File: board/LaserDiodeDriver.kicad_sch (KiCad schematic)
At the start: 55 parts, among them J1 Conn_01x02, K1 EE2-12NU, Q1 2N7002, Q2 IRF9Z34, SW1 SW_SPDT, U1 LT1009, U2 OPA4192, U3 LM317

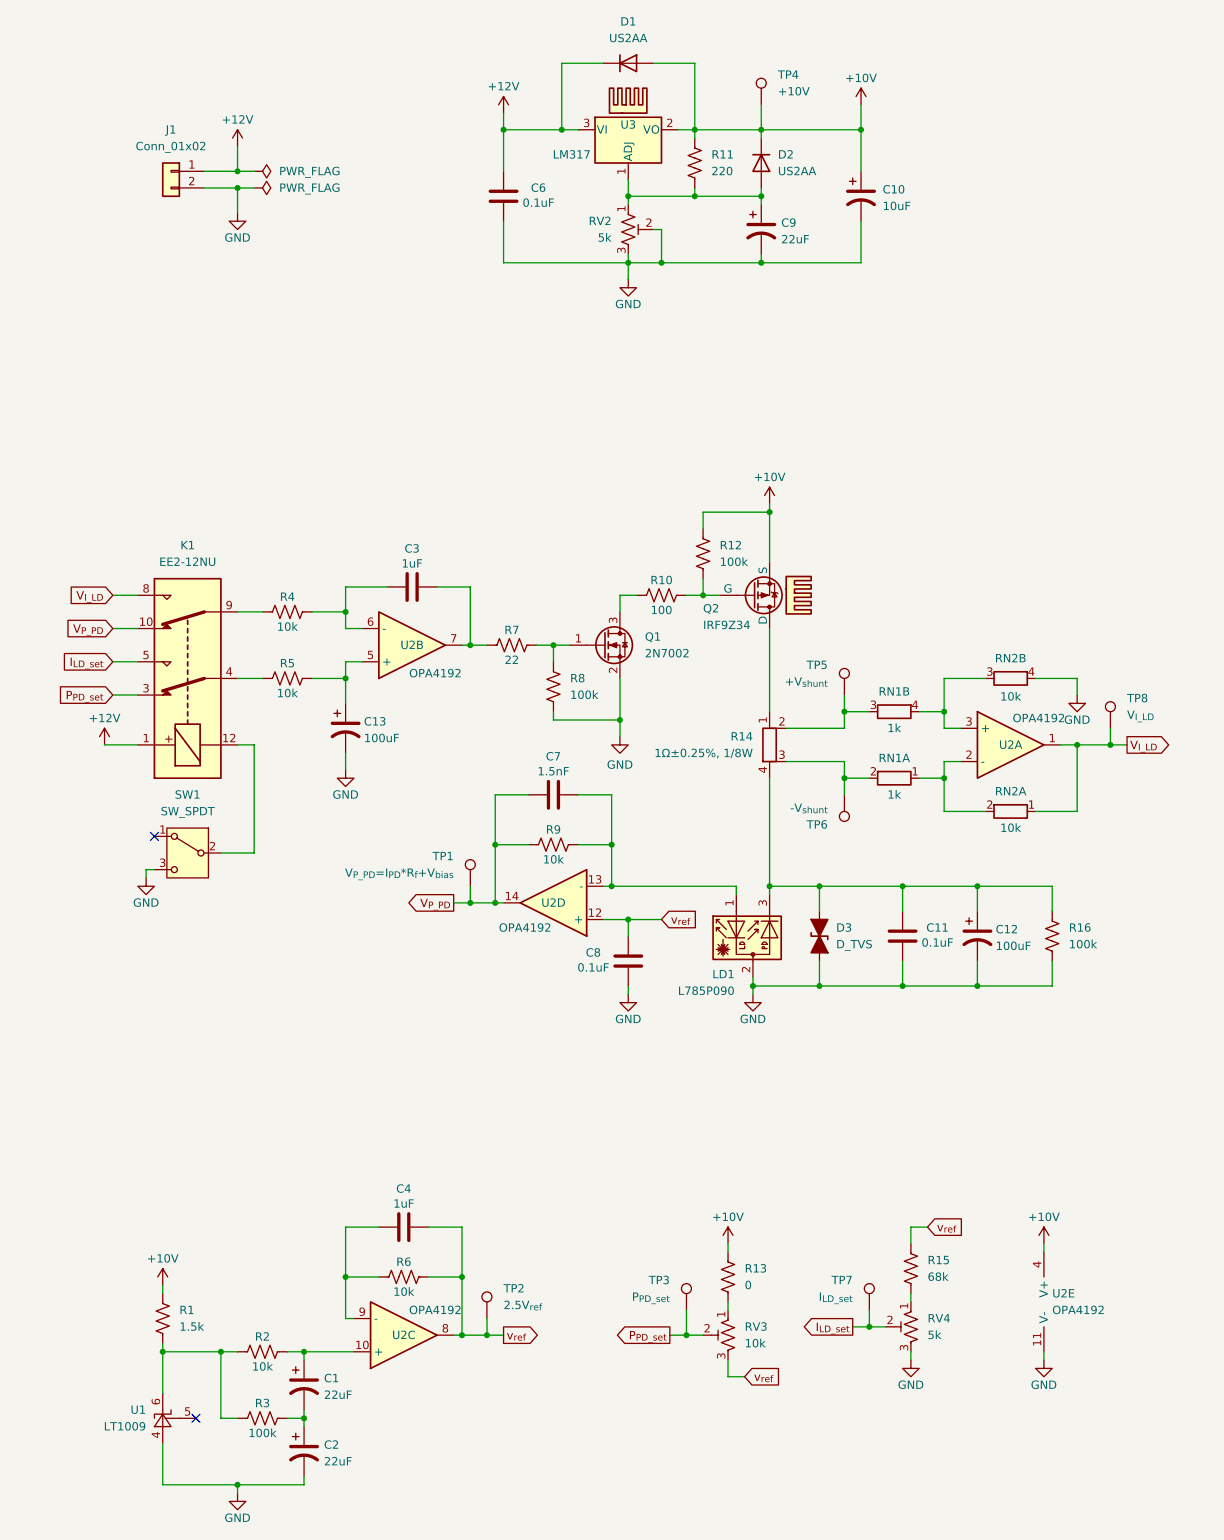
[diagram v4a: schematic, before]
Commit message: Various changes + component placement
* Removed signal relay in favor of SPDT switch in the interest of space.
* Placed components for optimal mechanical mounting with LD in center of PCB.
* Got rid of LM317 pot for space calculated proper values for LM317 to be +10V output.
* Arranged resistors for good placement.
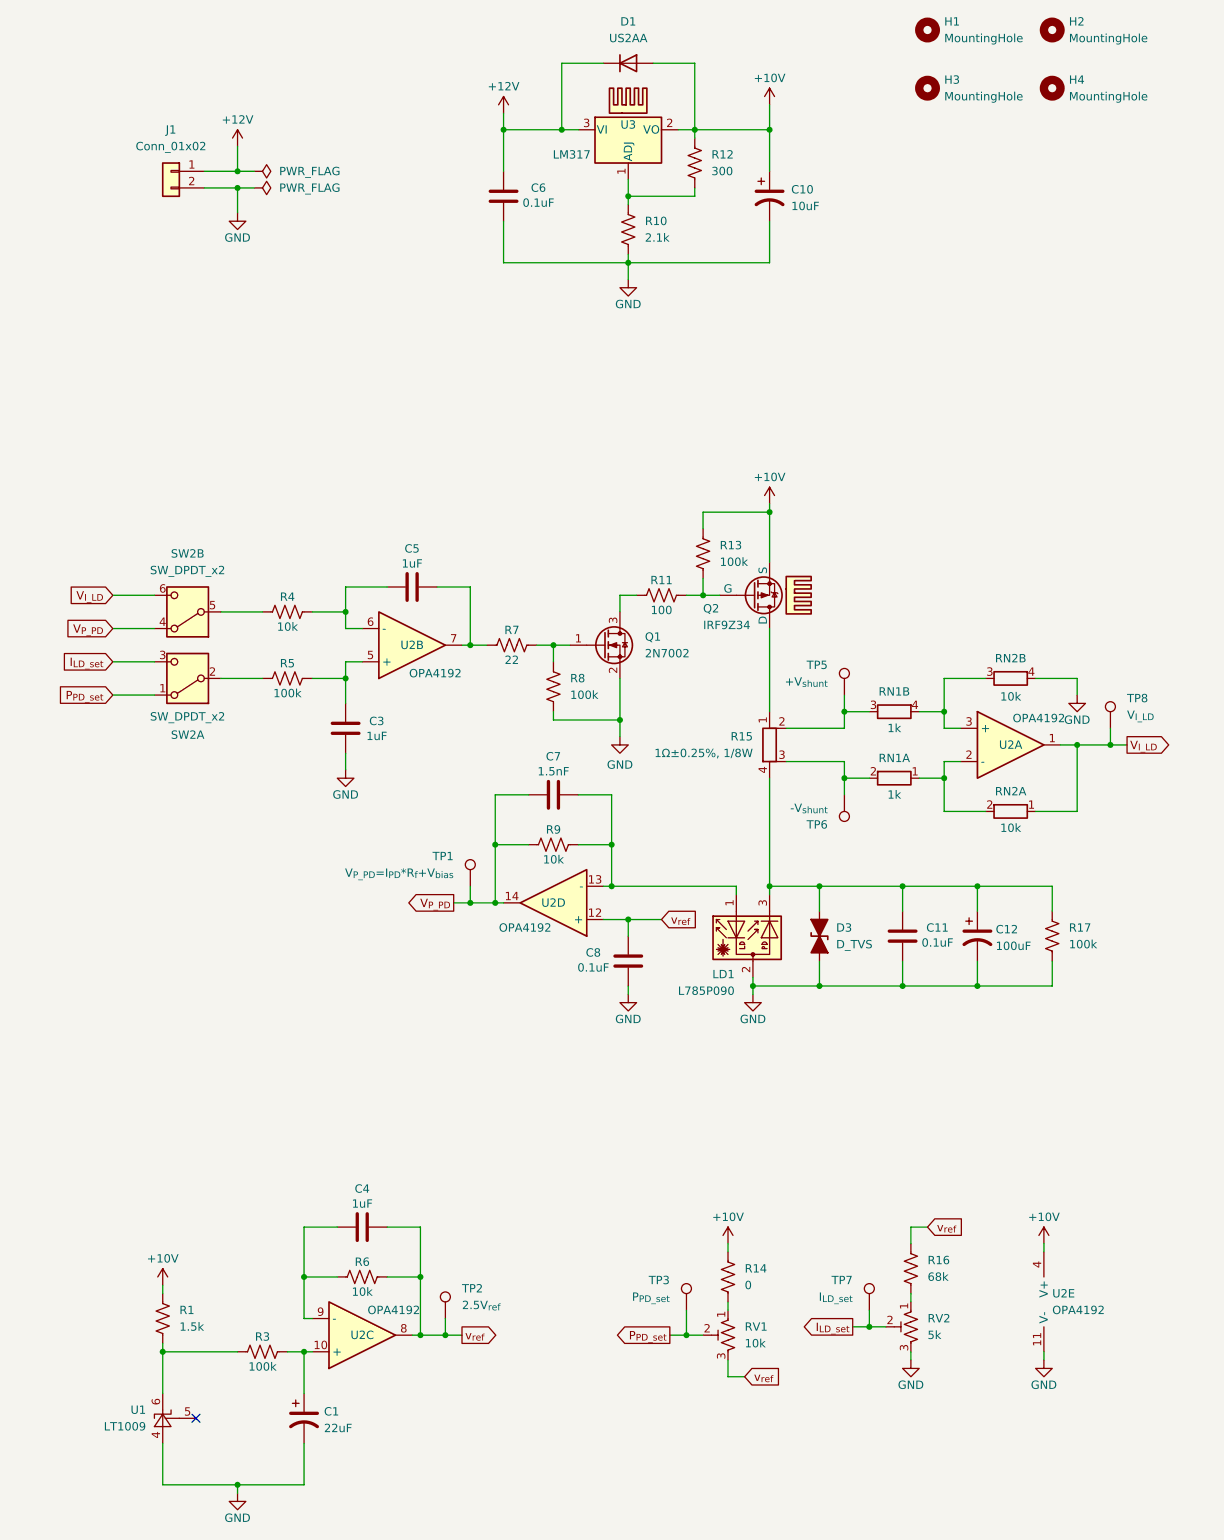
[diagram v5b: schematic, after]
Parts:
- removed C13: 100uF, Capacitor_SMD:CP_Elec_6.3x5.8, symbol Device:C_Polarized_US
- removed C2, C9: 22uF, Capacitor_SMD:CP_Elec_5x5.8, symbol Device:C_Polarized_US
- removed D2: US2AA, Diode_SMD:D_SMA, symbol Diode:US2AA
- removed K1: EE2-12NU, Relay_SMD:Relay_DPDT_Kemet_EE2_NU, symbol Relay:EE2-12NU
- removed R2: 10k, Resistor_SMD:R_0603_1608Metric, symbol Device:R_US
- removed RV2: 5k, Potentiometer_THT:Potentiometer_Bourns_3296Y_Vertical, symbol Device:R_Potentiometer_Trim_US
- removed SW1: SW_SPDT, Button_Switch_THT:SW_Slide_SPDT_Straight_CK_OS102011MS2Q, symbol Switch:SW_SPDT
- removed TP4: +10V, TestPoint:TestPoint_Pad_D1.5mm, symbol Connector:TestPoint
- added C3: 1uF, Capacitor_SMD:C_0603_1608Metric, symbol Device:C
- added H1: MountingHole, Mounting_Wuerth:Mounting_Wuerth_WA-SMSI-M1.6_H5mm_ThreadDepth2mm_97730506334, symbol Mechanical:MountingHole
- added H2, H3, H4: MountingHole, symbol Mechanical:MountingHole
- added R10: 2.1k, Resistor_SMD:R_0603_1608Metric, symbol Device:R_US
- added SW2: SW_DPDT_x2, Button_Switch_SMD:SW_DPDT_CK_JS202011JCQN, symbol Switch:SW_DPDT_x2
- R12: renamed from R11; value 220 -> 300; Price (none) -> $0.23000
- R5: value 10k -> 100k
- renumbered C3 to C5, HS2 to HS1, HS1 to HS2, R10 to R11, R12 to R13, R13 to R14, R14 to R15, R15 to R16, R16 to R17, RV3 to RV1, RV4 to RV2
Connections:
- net GND: now also C1.2, C3.1, R10.2
- net I_{LD_set}: now also SW2.3 (C)
- net P_{PD_set}: now also SW2.1 (A)
- net V_{I_LD}: now also SW2.6 (C)
- net V_{P_PD}: now also SW2.4 (A)
- net at C1.1, U2.10 (+): now also R3.2
- net at R12.2, U3.1 (ADJ): now also R10.1
- net at R5.2, U2.5 (+): now also C3.2
- net at R4.1: now also SW2.5 (B)
- net at R5.1: now also SW2.2 (B)
- no-connect marks 2 -> 1
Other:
- moved on the sheet: C1, C10, C4, R3, R6, TP2, U2C

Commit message: Finished Layout
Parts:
- removed HS1, HS2: Heatsink, symbol Mechanical:Heatsink
- H1: footprint Mounting_Wuerth:Mounting_Wuerth_WA-SMSI-M1.6_H5mm_ThreadDepth2mm_97730506334 -> Mounting_Wuerth:Mounting_Wuerth_WA-SMSI-M1.6_H4.5mm_ThreadDepth2mm_97730456332; Price (none) -> $0.88000
- H2, H3, H4: footprint (none) -> Mounting_Wuerth:Mounting_Wuerth_WA-SMSI-M1.6_H4.5mm_ThreadDepth2mm_97730456332; Price (none) -> $0.88000
- R16: footprint Capacitor_SMD:C_0603_1608Metric -> Capacitor_SMD:C_0603_1608Metric_Pad1.08x0.95mm_HandSolder
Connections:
- net GND: now also RV2.1; no longer RV2.3
- net v_{ref}: now also RV1.1; no longer RV1.3
- net at R14.2: now also RV1.3; no longer RV1.1
- net at R16.2: now also RV2.3; no longer RV2.1
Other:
- moved on the sheet: C1, D1, R1, RV1, RV2, U1

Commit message: Final touches :)
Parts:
- LD1: LD_Datasheet http://www.egismos.disonhu.com/laser/diode-package.htm -> https://www.thorlabs.com/thorproduct.cfm?partnumber=L785P090
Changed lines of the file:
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@@
 			)
 		)
-		(property "LD_Datasheet" "http://www.egismos.disonhu.com/laser/diode-package.htm"
+		(property "LD_Datasheet" "https://www.thorlabs.com/thorproduct.cfm?partnumber=L785P090"
 			(at 132.08 161.29 90)
 			(effects

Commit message: Final Final touches. Added indicator LEDs.
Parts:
- added D4: LED (Blue), LED_SMD:LED_0603_1608Metric, symbol Device:LED
- added D5: LED (Yellow), LED_SMD:LED_0603_1608Metric, symbol Device:LED
- added R18: 345, Resistor_SMD:R_0603_1608Metric, symbol Device:R_US
- added R2: 500, Resistor_SMD:R_0603_1608Metric, symbol Device:R_US
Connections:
- net +10V: now also R18.1
- net +12V: now also R2.1
- net GND: now also D4.1 (K), D5.1 (K)
- new net: D5.2 (A), R2.2
- new net: D4.2 (A), R18.2
